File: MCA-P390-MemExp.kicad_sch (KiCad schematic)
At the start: 27 parts

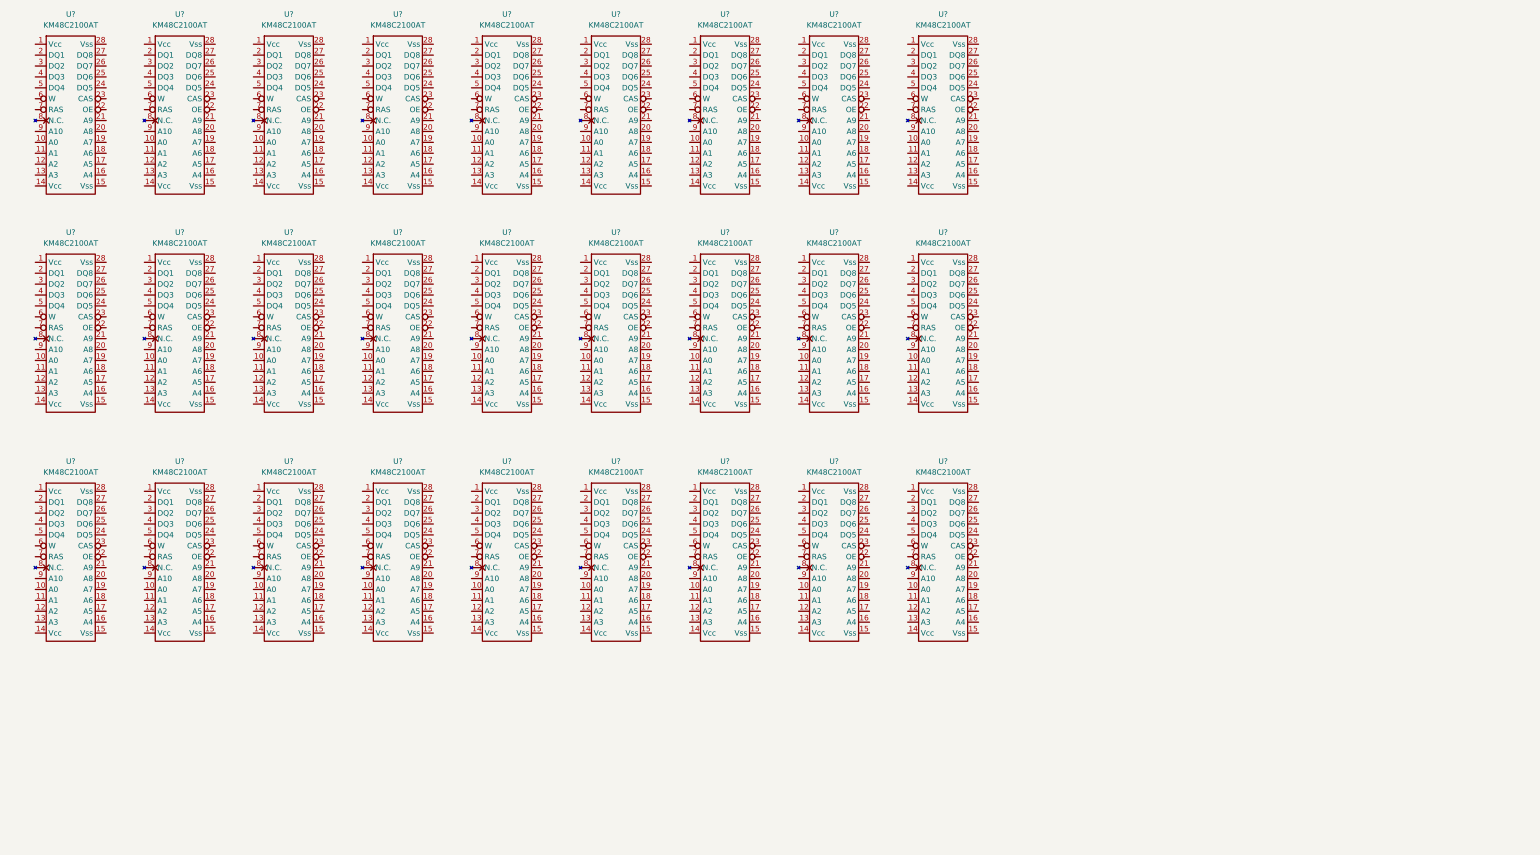
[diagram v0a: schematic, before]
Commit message: Adjustments to mem IC symbol, power, caps and ground for schematics
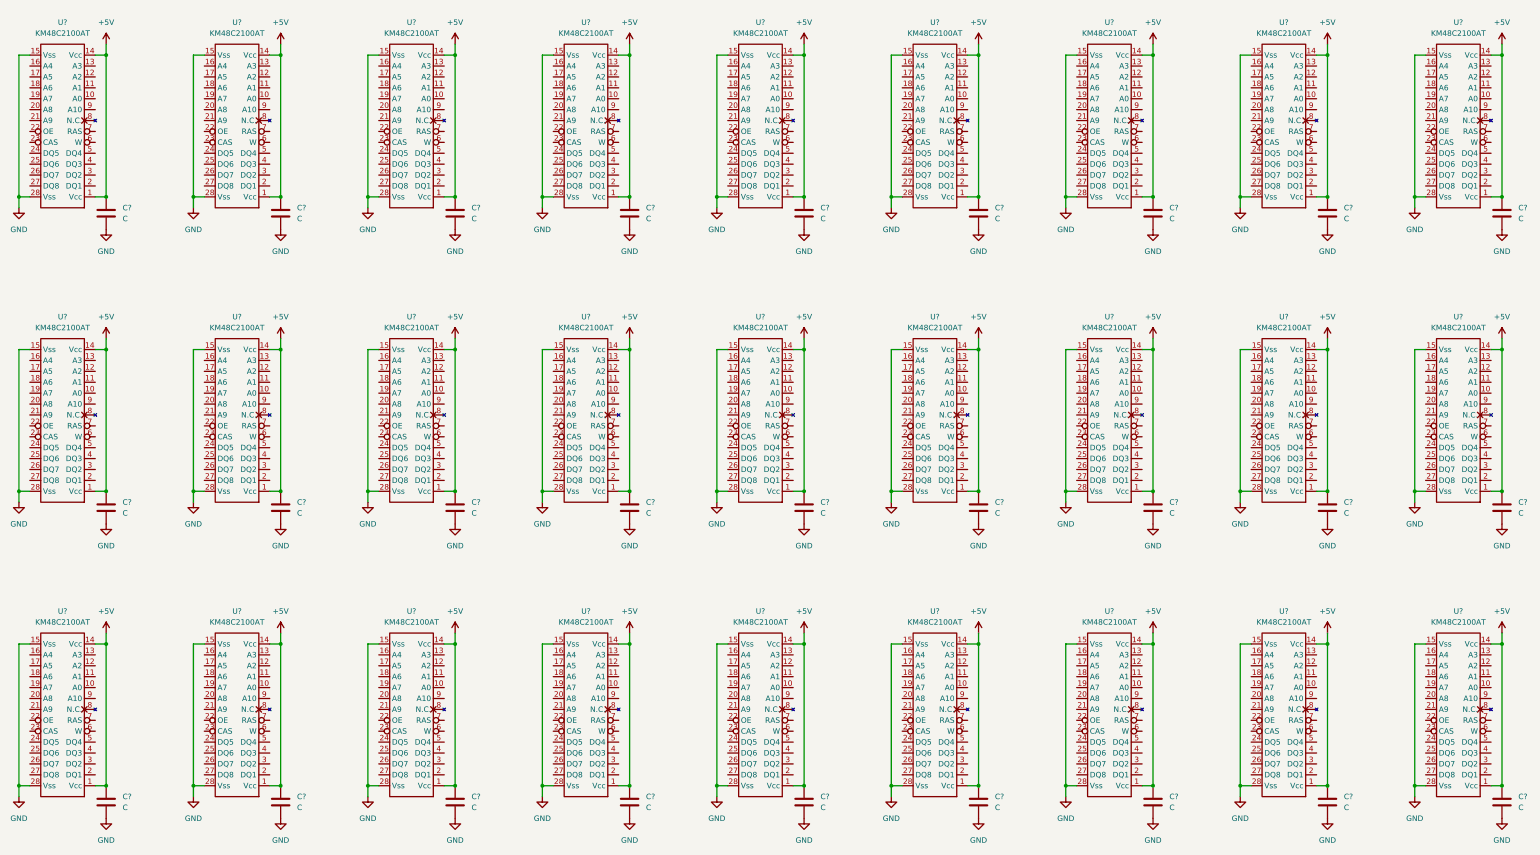
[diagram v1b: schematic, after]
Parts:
- removed U? (x27): KM48C2100AT, symbol P390_MCA_Memory_Board:KM48C2100AT
- added C? (x27): C, symbol Device:C
- added U? (x27): KM48C2100AT, symbol MCA-P390-MemExp:KM48C2100AT
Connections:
- new net +5V: C?.1, C?.1, C?.1, C?.1, C?.1, C?.1, C?.1, C?.1, C?.1, C?.1, C?.1, C?.1, C?.1, C?.1, C?.1, C?.1, C?.1, C?.1, C?.1, C?.1, C?.1, C?.1, C?.1, C?.1, C?.1, C?.1, C?.1, U?.1 (Vcc), U?.1 (Vcc), U?.1 (Vcc), U?.1 (Vcc), U?.1 (Vcc), U?.1 (Vcc), U?.1 (Vcc), U?.1 (Vcc), U?.1 (Vcc), U?.1 (Vcc), U?.1 (Vcc), U?.1 (Vcc), U?.1 (Vcc), U?.1 (Vcc), U?.1 (Vcc), U?.1 (Vcc), U?.1 (Vcc), U?.1 (Vcc), U?.1 (Vcc), U?.1 (Vcc), U?.1 (Vcc), U?.1 (Vcc), U?.1 (Vcc), U?.1 (Vcc), U?.1 (Vcc), U?.1 (Vcc), U?.1 (Vcc), U?.14 (Vcc), U?.14 (Vcc), U?.14 (Vcc), U?.14 (Vcc), U?.14 (Vcc), U?.14 (Vcc), U?.14 (Vcc), U?.14 (Vcc), U?.14 (Vcc), U?.14 (Vcc), U?.14 (Vcc), U?.14 (Vcc), U?.14 (Vcc), U?.14 (Vcc), U?.14 (Vcc), U?.14 (Vcc), U?.14 (Vcc), U?.14 (Vcc), U?.14 (Vcc), U?.14 (Vcc), U?.14 (Vcc), U?.14 (Vcc), U?.14 (Vcc), U?.14 (Vcc), U?.14 (Vcc), U?.14 (Vcc), U?.14 (Vcc)
- new net GND: C?.2, C?.2, C?.2, C?.2, C?.2, C?.2, C?.2, C?.2, C?.2, C?.2, C?.2, C?.2, C?.2, C?.2, C?.2, C?.2, C?.2, C?.2, C?.2, C?.2, C?.2, C?.2, C?.2, C?.2, C?.2, C?.2, C?.2, U?.15 (Vss), U?.15 (Vss), U?.15 (Vss), U?.15 (Vss), U?.15 (Vss), U?.15 (Vss), U?.15 (Vss), U?.15 (Vss), U?.15 (Vss), U?.15 (Vss), U?.15 (Vss), U?.15 (Vss), U?.15 (Vss), U?.15 (Vss), U?.15 (Vss), U?.15 (Vss), U?.15 (Vss), U?.15 (Vss), U?.15 (Vss), U?.15 (Vss), U?.15 (Vss), U?.15 (Vss), U?.15 (Vss), U?.15 (Vss), U?.15 (Vss), U?.15 (Vss), U?.15 (Vss), U?.28 (Vss), U?.28 (Vss), U?.28 (Vss), U?.28 (Vss), U?.28 (Vss), U?.28 (Vss), U?.28 (Vss), U?.28 (Vss), U?.28 (Vss), U?.28 (Vss), U?.28 (Vss), U?.28 (Vss), U?.28 (Vss), U?.28 (Vss), U?.28 (Vss), U?.28 (Vss), U?.28 (Vss), U?.28 (Vss), U?.28 (Vss), U?.28 (Vss), U?.28 (Vss), U?.28 (Vss), U?.28 (Vss), U?.28 (Vss), U?.28 (Vss), U?.28 (Vss), U?.28 (Vss)
